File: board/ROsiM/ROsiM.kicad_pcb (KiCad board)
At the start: 2 copper layers, 170.2 x 78.7 mm, 92 parts, among them J1 AVR-ISP-6, J2 USB_B, J4 EXT_ADDR, J5 EXT_D, J6 External ~RESET, J7 External RESET, Q1 2N3904, Q2 2N3906, SW1 SW_Push, U1 ATmega328P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

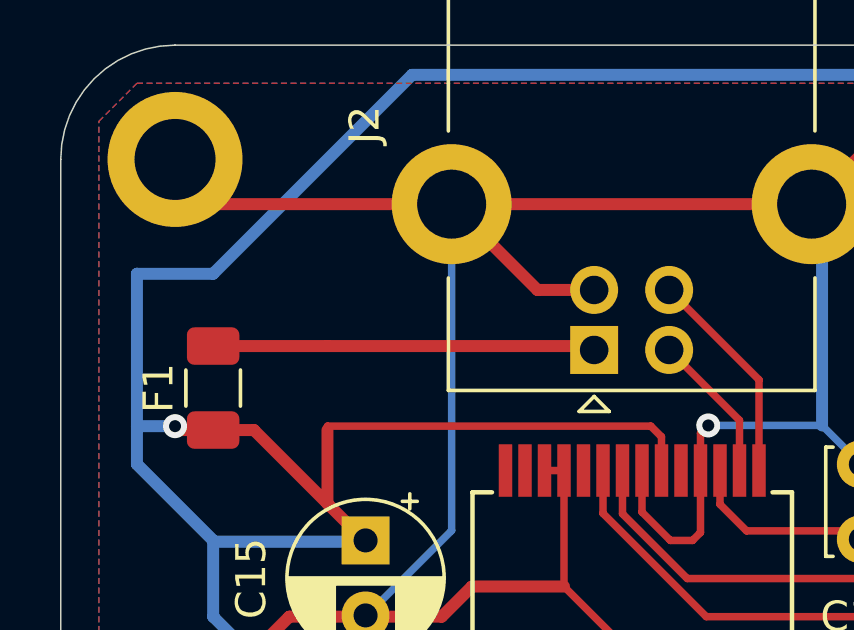
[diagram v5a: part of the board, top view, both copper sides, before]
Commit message: Added schottky diode on USB +5v input
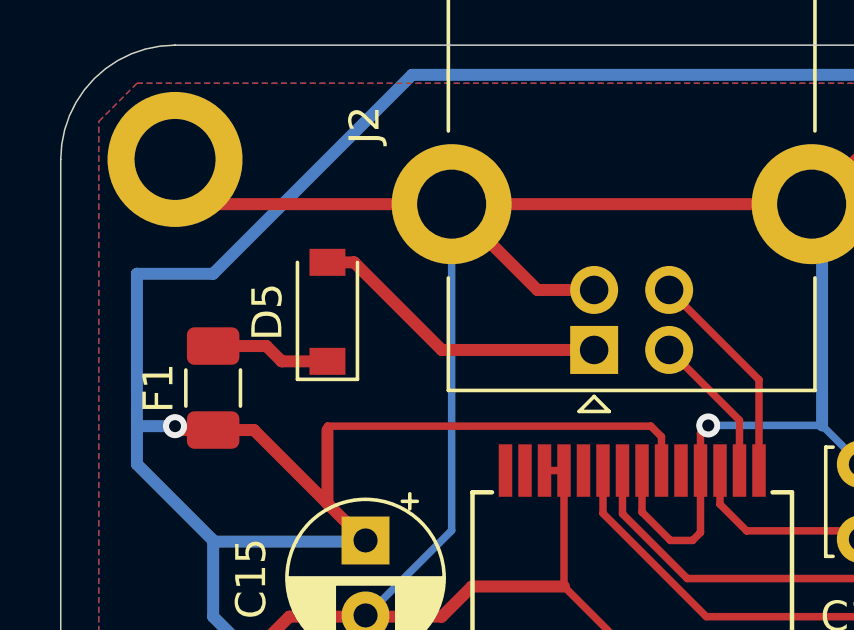
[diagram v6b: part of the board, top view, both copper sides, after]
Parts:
- added D5: BAT48ZFILM, Diode_SMD:D_SOD-123, F.Cu at (100.3, 63.5)
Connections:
- F1 pad 2: Net-(F1-Pad2) -> Net-(D5-Pad1)
- J2 pad 1: Net-(F1-Pad2) -> Net-(D5-Pad2)
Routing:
- net Net-(F1-Pad2): track 12.8 -> 0.00 mm
- net Net-(D5-Pad2): track 0.00 -> 10.3 mm
- net Net-(D5-Pad1): track 0.00 -> 4.02 mm
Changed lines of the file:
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@@
-(kicad_pcb (version 20171130) (host pcbnew 5.1.8-4.fc33)
+(kicad_pcb (version 20171130) (host pcbnew 5.1.9-1.fc33)
   (general
     (thickness 1.6)
     (drawings 67)
-    (tracks 3424)
+    (tracks 3428)
     (zones 0)
-    (modules 92)
-    (nets 144)
+    (modules 93)
+    (nets 145)
   )
   (page A4)
@@
   (net 138 "Net-(D4-Pad2)")
   (net 139 "Net-(D4-Pad1)")
-  (net 140 "Net-(F1-Pad2)")
-  (net 141 "Net-(J2-Pad3)")
-  (net 142 "Net-(J2-Pad2)")
-  (net 143 "Net-(C29-Pad1)")
+  (net 140 "Net-(J2-Pad3)")
+  (net 141 "Net-(J2-Pad2)")
+  (net 142 "Net-(C29-Pad1)")
+  (net 143 "Net-(D5-Pad2)")
+  (net 144 "Net-(D5-Pad1)")
   (net_class Default "This is the default net class."
     (clearance 0.2)
@@
     (uvia_drill 0.1)
     (add_net GND)
-    (add_net "Net-(F1-Pad2)")
+    (add_net "Net-(D5-Pad1)")
+    (add_net "Net-(D5-Pad2)")
     (add_net VCC)
   )
+  (module Diode_SMD:D_SOD-123 (layer F.Cu)
+    (at 100.33 63.5 90)
+    (descr SOD-123)
+    (tags SOD-123)
+    (attr smd)
+    (fp_text reference D5 (at 0 -2 90) (layer F.SilkS)
+      (effects (font (size 1 1) (thickness 0.15)))
+    )
+    (fp_text value BAT48ZFILM (at 0 2.1 90) (layer F.Fab)
+      (effects (font (size 1 1) (thickness 0.15)))
+    )
+    (fp_line (start -2.25 -1) (end 1.65 -1) (layer F.SilkS) (width 0.12))
+    (fp_line (start -2.25 1) (end 1.65 1) (layer F.SilkS) (width 0.12))
+    (fp_line (start -2.35 -1.15) (end -2.35 1.15) (layer F.CrtYd) (width 0.05))
+    (fp_line (start 2.35 1.15) (end -2.35 1.15) (layer F.CrtYd) (width 0.05))
+    (fp_line (start 2.35 -1.15) (end 2.35 1.15) (layer F.CrtYd) (width 0.05))
+    (fp_line (start -2.35 -1.15) (end 2.35 -1.15) (layer F.CrtYd) (width 0.05))
+    (fp_line (start -1.4 -0.9) (end 1.4 -0.9) (layer F.Fab) (width 0.1))
+    (fp_line (start 1.4 -0.9) (end 1.4 0.9) (layer F.Fab) (width 0.1))
+    (fp_line (start 1.4 0.9) (end -1.4 0.9) (layer F.Fab) (width 0.1))
+    (fp_line (start -1.4 0.9) (end -1.4 -0.9) (layer F.Fab) (width 0.1))
+    (fp_line (start -0.75 0) (end -0.35 0) (layer F.Fab) (width 0.1))
+    (fp_line (start -0.35 0) (end -0.35 -0.55) (layer F.Fab) (width 0.1))
+    (fp_line (start -0.35 0) (end -0.35 0.55) (layer F.Fab) (width 0.1))
+    (fp_line (start -0.35 0) (end 0.25 -0.4) (layer F.Fab) (width 0.1))
+    (fp_line (start 0.25 -0.4) (end 0.25 0.4) (layer F.Fab) (width 0.1))
+    (fp_line (start 0.25 0.4) (end -0.35 0) (layer F.Fab) (width 0.1))
+    (fp_line (start 0.25 0) (end 0.75 0) (layer F.Fab) (width 0.1))
+    (fp_line (start -2.25 -1) (end -2.25 1) (layer F.SilkS) (width 0.12))
+    (fp_text user %R (at 0 -2 90) (layer F.Fab)
+      (effects (font (size 1 1) (thickness 0.15)))
+    )
+    (pad 2 smd rect (at 1.65 0 90) (size 0.9 1.2) (layers F.Cu F.Paste F.Mask)
+      (net 143 "Net-(D5-Pad2)"))
+    (pad 1 smd rect (at -1.65 0 90) (size 0.9 1.2) (layers F.Cu F.Paste F.Mask)
+      (net 144 "Net-(D5-Pad1)"))
+    (model ${KISYS3DMOD}/Diode_SMD.3dshapes/D_SOD-123.wrl
+      (at (xyz 0 0 0))
+      (scale (xyz 1 1 1))
+      (rotate (xyz 0 0 0))
+    )
+  )
   (module Capacitor_THT:C_Disc_D3.4mm_W2.1mm_P2.50mm (layer F.Cu)
     (at 102.87 77.47 270)
@@
       (net 4 /~RESET))
     (pad 1 thru_hole circle (at 0 0 270) (size 1.6 1.6) (drill 0.8) (layers *.Cu *.Mask)
-      (net 143 "Net-(C29-Pad1)"))
+      (net 142 "Net-(C29-Pad1)"))
     (model ${KISYS3DMOD}/Capacitor_THT.3dshapes/C_Disc_D3.4mm_W2.1mm_P2.50mm.wrl
       (at (xyz 0 0 0))
@@
       (net 2 GND))
     (pad 3 thru_hole circle (at 2 2.5 180) (size 1.6 1.6) (drill 0.95) (layers *.Cu *.Mask)
-      (net 141 "Net-(J2-Pad3)"))
+      (net 140 "Net-(J2-Pad3)"))
     (pad 2 thru_hole circle (at 0 2.5 180) (size 1.6 1.6) (drill 0.95) (layers *.Cu *.Mask)
-      (net 142 "Net-(J2-Pad2)"))
+      (net 141 "Net-(J2-Pad2)"))
     (pad 1 thru_hole rect (at 0 0 180) (size 1.6 1.6) (drill 0.95) (layers *.Cu *.Mask)
-      (net 140 "Net-(F1-Pad2)"))
+      (net 143 "Net-(D5-Pad2)"))
     (model ${KISYS3DMOD}/Connector_USB.3dshapes/USB_B_Lumberg_2411_02_Horizontal.wrl
       (at (xyz 0 0 0))
@@
       (net 135 +3V3))
     (pad 16 smd rect (at 3.6 3.575 90) (size 1.75 0.45) (layers F.Cu F.Paste F.Mask)
-      (net 142 "Net-(J2-Pad2)"))
+      (net 141 "Net-(J2-Pad2)"))
     (pad 15 smd rect (at 3.6 4.225 90) (size 1.75 0.45) (layers F.Cu F.Paste F.Mask)
-      (net 141 "Net-(J2-Pad3)"))
+      (net 140 "Net-(J2-Pad3)"))
     (pad 14 smd rect (at -3.6 4.225 90) (size 1.75 0.45) (layers F.Cu F.Paste F.Mask))
     (pad 13 smd rect (at -3.6 3.575 90) (size 1.75 0.45) (layers F.Cu F.Paste F.Mask))
@@
     (pad 3 smd rect (at -3.6 -2.925 90) (size 1.75 0.45) (layers F.Cu F.Paste F.Mask))
     (pad 2 smd rect (at -3.6 -3.575 90) (size 1.75 0.45) (layers F.Cu F.Paste F.Mask)
-      (net 143 "Net-(C29-Pad1)"))
+      (net 142 "Net-(C29-Pad1)"))
     (pad 1 smd rect (at -3.6 -4.225 90) (size 1.75 0.45) (layers F.Cu F.Paste F.Mask)
       (net 12 /TTL-RX))
@@
     )
     (pad 2 smd roundrect (at 1.4 0 90) (size 1.25 1.75) (layers F.Cu F.Paste F.Mask) (roundrect_rratio 0.2)
-      (net 140 "Net-(F1-Pad2)"))
+      (net 144 "Net-(D5-Pad1)"))
     (pad 1 smd roundrect (at -1.4 0 90) (size 1.25 1.75) (layers F.Cu F.Paste F.Mask) (roundrect_rratio 0.2)
       (net 5 VCC))
@@
   (segment (start 96.52 71.12) (end 96.52 73.66) (width 0.4) (layer B.Cu) (net 5))
   (segment (start 96.56 71.16) (end 96.52 71.12) (width 0.4) (layer B.Cu) (net 5))
+  (segment (start 108.182 75.9575) (end 108.215 75.99) (width 0.25) (layer F.Cu) (net 5))
+  (segment (start 109.22 80.01) (end 107.95 78.74) (width 0.4) (layer F.Cu) (net 5))
+  (segment (start 107.95 78.74) (end 107.95 78.105) (width 0.4) (layer F.Cu) (net 5))
+  (segment (start 108.215 77.84) (end 107.95 78.105) (width 0.25) (layer F.Cu) (net 5))
+  (segment (start 108.215 75.99) (end 108.215 77.84) (width 0.25) (layer F.Cu) (net 5))
   (segment (start 97.79 110.49) (end 111.905 110.49) (width 0.25) (layer F.Cu) (net 6))
   (segment (start 111.905 110.49) (end 115.715 114.3) (width 0.25) (layer F.Cu) (net 6))
@@
   (segment (start 124.46 72.39) (end 127 69.85) (width 0.25) (layer F.Cu) (net 139))
   (segment (start 127 69.85) (end 127 60.96) (width 0.25) (layer F.Cu) (net 139))
-  (segment (start 100.33 64.64) (end 109.09 64.64) (width 0.4) (layer F.Cu) (net 140))
-  (segment (start 109.09 64.64) (end 109.22 64.77) (width 0.4) (layer F.Cu) (net 140))
-  (segment (start 100.33 64.64) (end 96.52 64.64) (width 0.4) (layer F.Cu) (net 140))
-  (segment (start 111.72 62.77) (end 114.715 65.765) (width 0.25) (layer F.Cu) (net 141))
-  (segment (start 114.715 65.765) (end 114.715 68.79) (width 0.25) (layer F.Cu) (net 141))
-  (segment (start 111.72 64.77) (end 114.065 67.115) (width 0.25) (layer F.Cu) (net 142))
-  (segment (start 114.065 67.115) (end 114.065 68.79) (width 0.25) (layer F.Cu) (net 142))
-  (segment (start 108.182 75.9575) (end 108.215 75.99) (width 0.25) (layer F.Cu) (net 5))
-  (segment (start 109.22 80.01) (end 107.95 78.74) (width 0.4) (layer F.Cu) (net 5))
-  (segment (start 107.95 78.74) (end 107.95 78.105) (width 0.4) (layer F.Cu) (net 5))
-  (segment (start 108.215 77.84) (end 107.95 78.105) (width 0.25) (layer F.Cu) (net 5))
-  (segment (start 108.215 75.99) (end 108.215 77.84) (width 0.25) (layer F.Cu) (net 5))
-  (segment (start 106.915 74.954998) (end 106.915 75.99) (width 0.25) (layer F.Cu) (net 143))
-  (segment (start 106.750001 74.789999) (end 106.915 74.954998) (width 0.25) (layer F.Cu) (net 143))
-  (segment (start 105.550001 74.789999) (end 106.750001 74.789999) (width 0.25) (layer F.Cu) (net 143))
-  (segment (start 102.87 77.47) (end 105.550001 74.789999) (width 0.25) (layer F.Cu) (net 143))
+  (segment (start 109.09 64.64) (end 109.22 64.77) (width 0.4) (layer F.Cu) (net 143))
+  (segment (start 111.72 62.77) (end 114.715 65.765) (width 0.25) (layer F.Cu) (net 140))
+  (segment (start 114.715 65.765) (end 114.715 68.79) (width 0.25) (layer F.Cu) (net 140))
+  (segment (start 111.72 64.77) (end 114.065 67.115) (width 0.25) (layer F.Cu) (net 141))
+  (segment (start 114.065 67.115) (end 114.065 68.79) (width 0.25) (layer F.Cu) (net 141))
+  (segment (start 106.915 74.954998) (end 106.915 75.99) (width 0.25) (layer F.Cu) (net 142))
+  (segment (start 106.750001 74.789999) (end 106.915 74.954998) (width 0.25) (layer F.Cu) (net 142))
+  (segment (start 105.550001 74.789999) (end 106.750001 74.789999) (width 0.25) (layer F.Cu) (net 142))
+  (segment (start 102.87 77.47) (end 105.550001 74.789999) (width 0.25) (layer F.Cu) (net 142))
+  (segment (start 100.33 61.85) (end 101.22 61.85) (width 0.4) (layer F.Cu) (net 143))
+  (segment (start 104.14 64.77) (end 109.22 64.77) (width 0.4) (layer F.Cu) (net 143))
+  (segment (start 101.22 61.85) (end 104.14 64.77) (width 0.4) (layer F.Cu) (net 143))
+  (segment (start 100.33 65.15) (end 98.805 65.15) (width 0.4) (layer F.Cu) (net 144))
+  (segment (start 98.295 64.64) (end 96.52 64.64) (width 0.4) (layer F.Cu) (net 144))
+  (segment (start 98.805 65.15) (end 98.295 64.64) (width 0.4) (layer F.Cu) (net 144))
   (zone (net 2) (net_name GND) (layer B.Cu) (hatch edge 0.508)
     (connect_pads (clearance 0.508))

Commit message: Lower specification of F1 to 200mA, to stay under BAT48 max current
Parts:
- F1: value 500mA -> 200mA

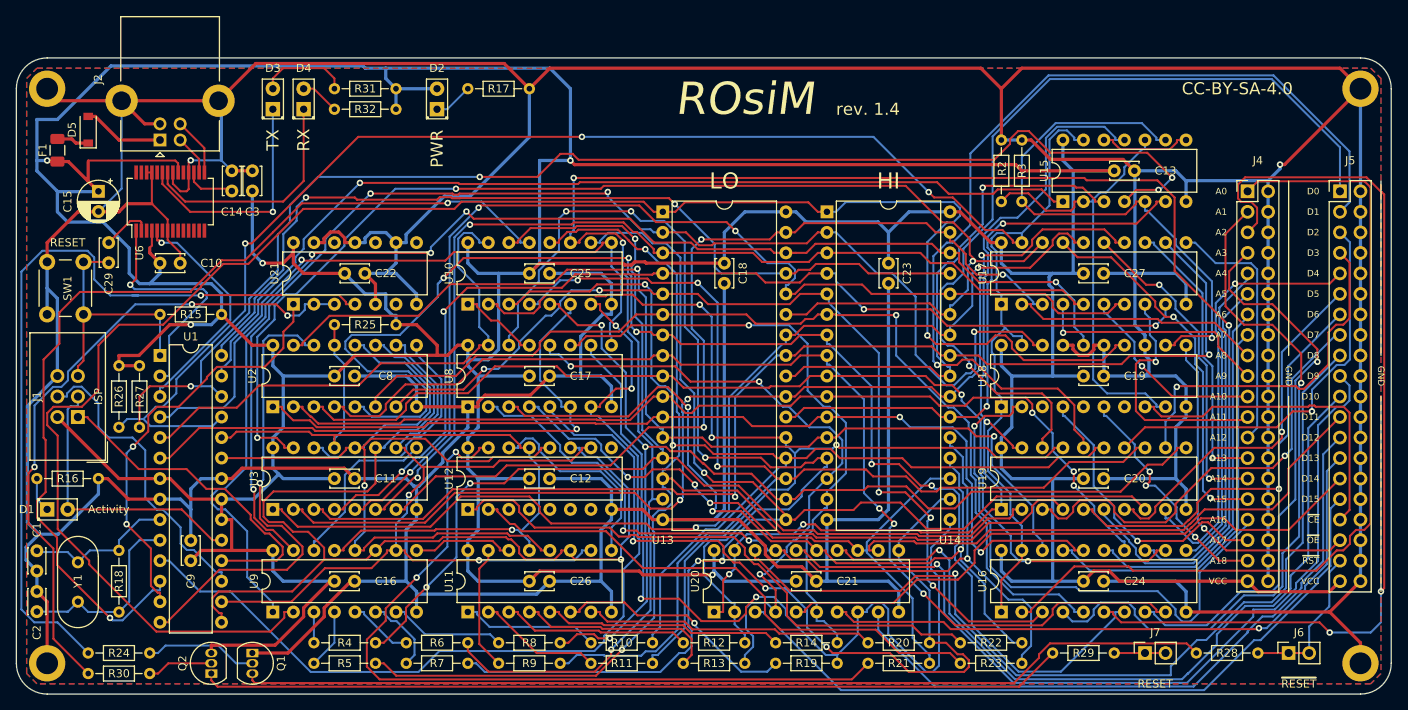
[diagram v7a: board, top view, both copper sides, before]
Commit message: Update part of the project for kicad 7
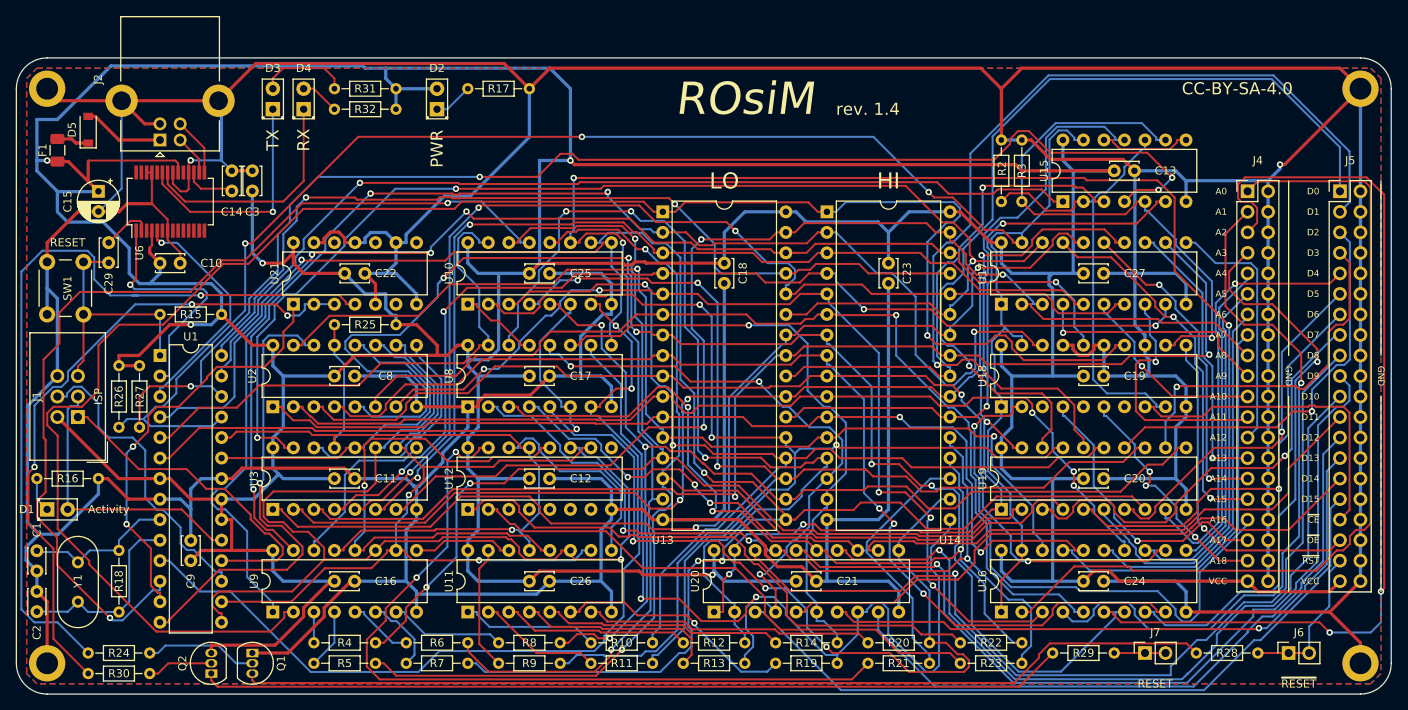
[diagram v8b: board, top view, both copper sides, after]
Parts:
- J6: value External ~RESET -> External ~{RESET}
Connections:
- net /~ERST renamed /~{ERST}
- net /~EXT_CE renamed /~{EXT_CE}
- net /~EXT_D_EN renamed /~{EXT_D_EN}
- net /~EXT_EN renamed /~{EXT_EN}
- net /~EXT_OE renamed /~{EXT_OE}
- net /~EXT_RESET renamed /~{EXT_RESET}
- net /~PISO_CLR renamed /~{PISO_CLR}
- net /~RESET renamed /~{RESET}
- net /~SIPO_CLR renamed /~{SIPO_CLR}
- net /~SIPO_OE renamed /~{SIPO_OE}
- net /~SRAM_CE renamed /~{SRAM_CE}
- net /~SRAM_CE_EXT renamed /~{SRAM_CE_EXT}
- net /~SRAM_CE_MCU renamed /~{SRAM_CE_MCU}
- net /~SRAM_OE renamed /~{SRAM_OE}
- net /~SRAM_OE_EXT renamed /~{SRAM_OE_EXT}
- net /~SRAM_OE_MCU renamed /~{SRAM_OE_MCU}
- net /~SRAM_WE renamed /~{SRAM_WE}
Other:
- net class Default removed
- net class POWER removed
- board text added: "~{CE}"
- board text added: "~{OE}"
- board text added: "~{RESET}"
- board text added: "~{RST}"
- board text removed: "~CE"
- board text removed: "~OE"
- board text removed: "~RESET"
- board text removed: "~RST"
